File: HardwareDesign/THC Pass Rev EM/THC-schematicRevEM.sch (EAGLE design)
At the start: 55 parts, among them J1 2.1MM-PLUG-PCB-MNT, J2 DB9-MALE, J3 DB9-FEMALE, Q1 2N2222A, U1 7805T

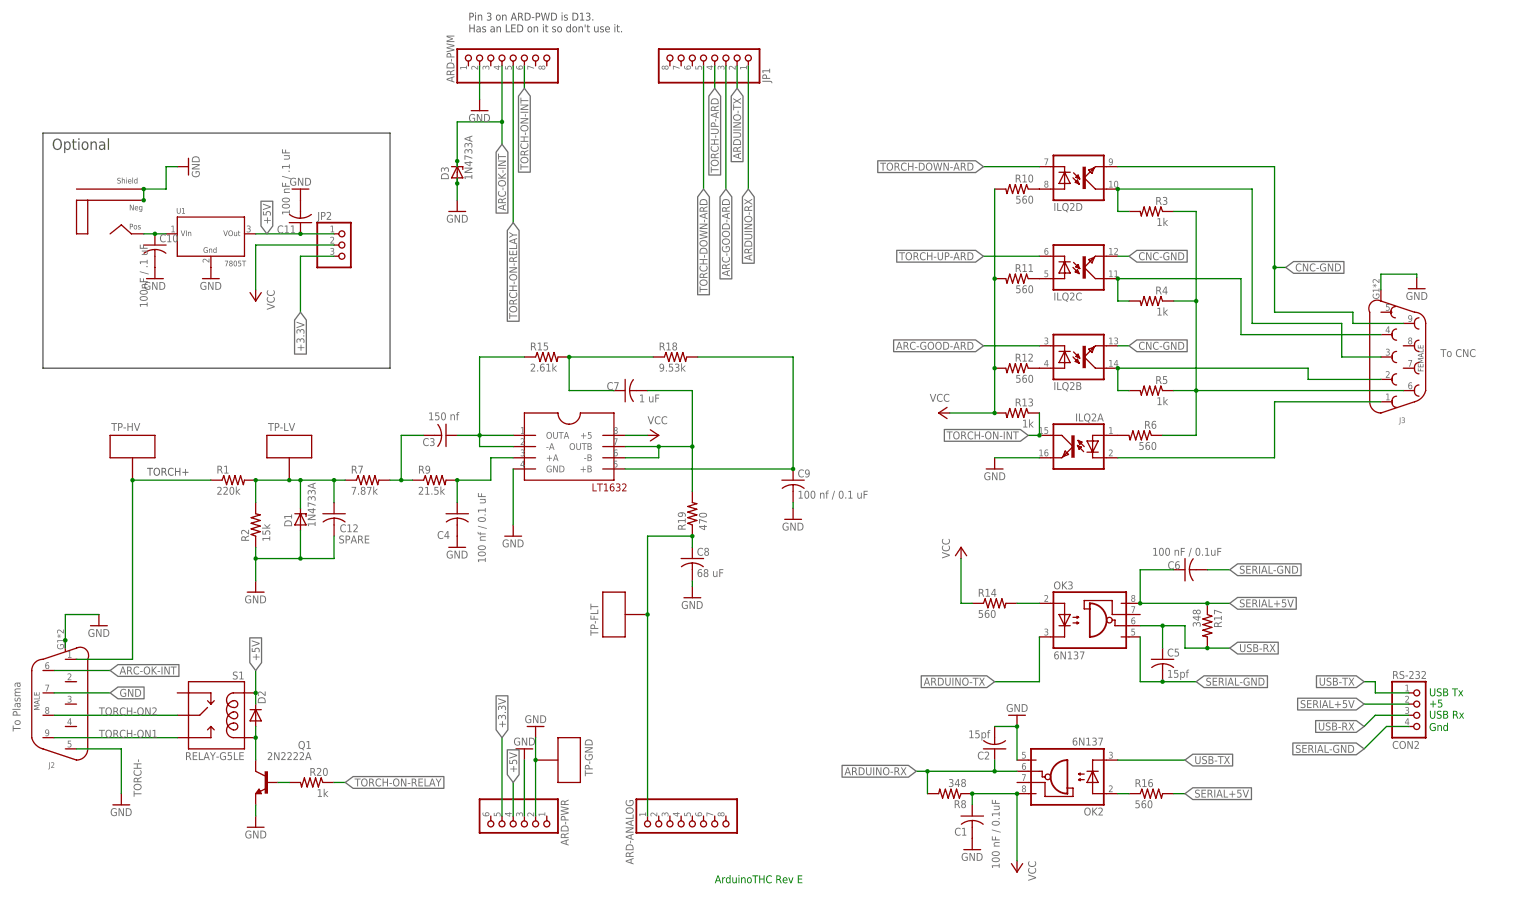
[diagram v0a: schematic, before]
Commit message: Added section to manual for programming the Arduino.  Cleaned up schematic files.
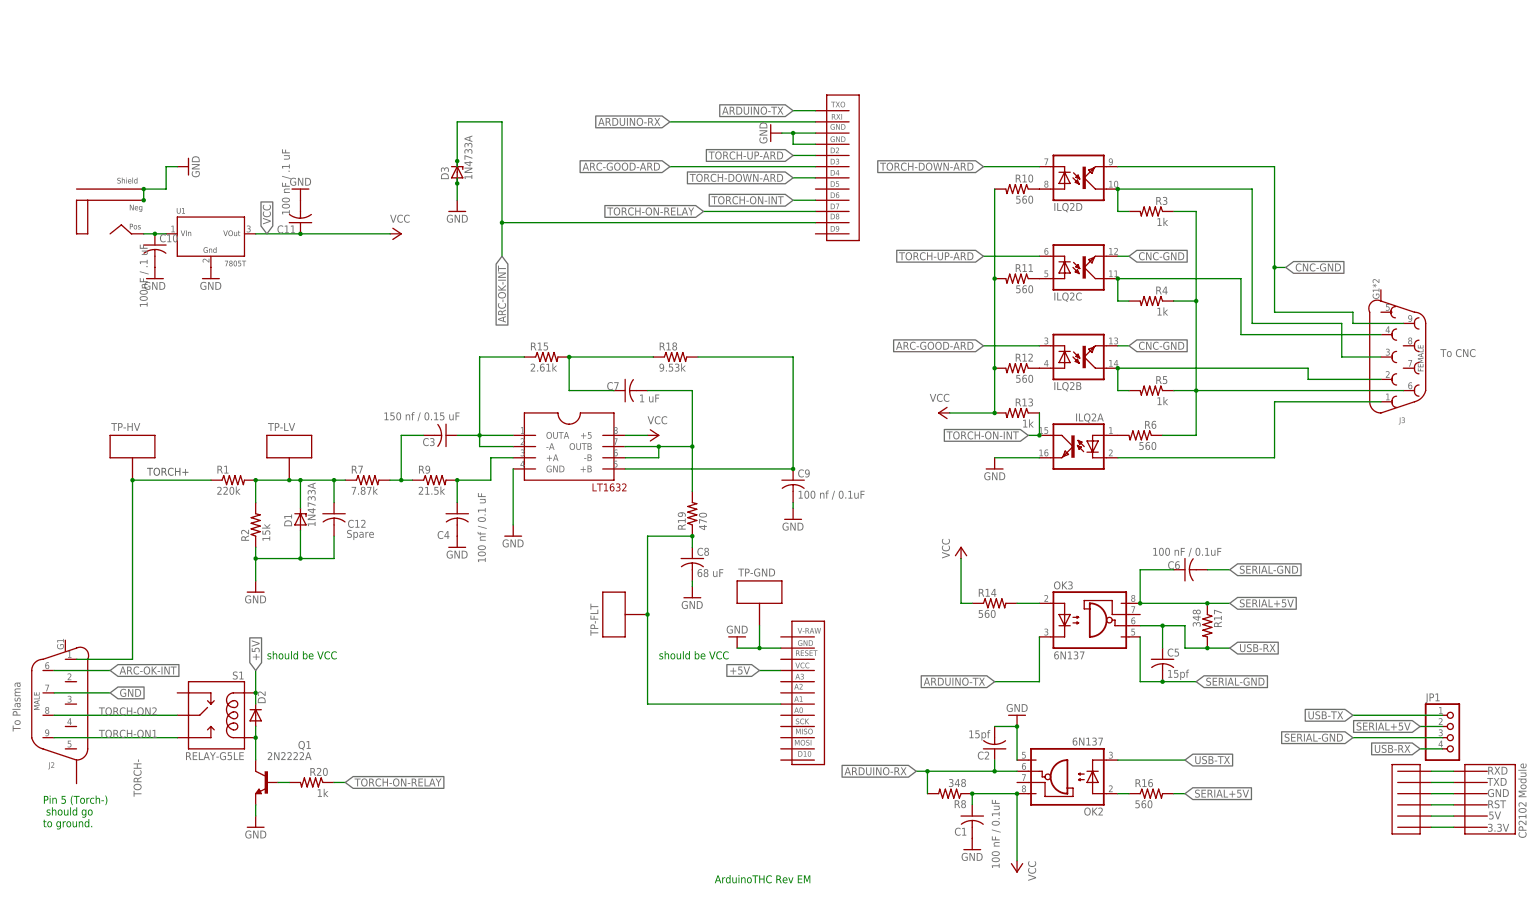
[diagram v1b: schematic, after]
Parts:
- removed ARD-ANALOG, ARD-PWM: (no value), pinhead:PINHD-1X8
- removed ARD-PWR: (no value), pinhead:PINHD-1X6
- removed JP2: (no value), pinhead:PINHD-1X3
- removed RS-232: CON2, pinhead:PINHD-1X4
- added MOD1: ARDUINO-PRO-MICRO-FOOTPRINT, ArduinoProMicro:ARDUINO-PRO-MICRO-FOOTPRINT
- added U$2: CP2102-TTL-USB, CP2102 TTL to USB:CP2102-TTL-USB
- added U$3: CP2102-PADS, CP2102 TTL to USB:CP2102-PADS
- C12: value SPARE -> Spare
- C3: value 150 nf -> 150 nf / 0.15 uF
- C9: value 100 nf / 0.1 uF -> 100 nf / 0.1uF
- JP1: device pinhead:PINHD-1X8 -> pinhead:PINHD-1X4
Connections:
- removed net +3.3V: ARD-PWR.5, JP2.3
- new net N$10: U$2.P$RST, U$3.P$RST
- new net N$11: U$2.P$TXD, U$3.P$TXD
- new net N$12: U$2.P$RXD, U$3.P$RXD
- new net N$13: U$2.P$GND, U$3.P$GND
- new net N$14: U$2.P$5V, U$3.P$5V
- new net N$6: U$2.P$3.3V, U$3.P$3.3V
- net +5V: now also MOD1G$1.VCC; no longer ARD-PWR.4, C11.1, JP2.1, U1.VOUT
- net ARC-GOOD-ARD: now also MOD1G$2.D3; no longer JP1.3
- net ARC-OK-INT: now also MOD1G$2.D8; no longer ARD-PWM.4
- net ARD-ANALOG-IN: now also MOD1G$1.A1; no longer ARD-ANALOG.1
- net ARDUINO-RX: now also MOD1G$2.RXI; no longer JP1.1
- net ARDUINO-TX: now also MOD1G$2.TX0; no longer JP1.2
- net GND: now also MOD1G$1.GND2, MOD1G$2.GND10, MOD1G$2.GND9; no longer ARD-PWM.2, ARD-PWR.2, ARD-PWR.3, J2.P$5, J2.P$SHLD, J3.P$SHLD
- net SERIAL+5V: now also JP1.2; no longer RS-232.2
- net SERIAL-GND: now also JP1.3; no longer RS-232.4
- net TORCH-DOWN-ARD: now also MOD1G$2.D4; no longer JP1.5
- net TORCH-ON-INT: now also MOD1G$2.D6; no longer ARD-PWM.6
- net TORCH-ON-RELAY: now also MOD1G$2.D7; no longer ARD-PWM.5
- net TORCH-UP-ARD: now also MOD1G$2.D2; no longer JP1.4
- net USB-RX: now also JP1.4; no longer RS-232.3
- net USB-TX: now also JP1.1; no longer RS-232.1
- net VCC: now also C11.1, U1.VOUT; no longer JP2.2
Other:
- note added: "ArduinoTHC Rev EM"
- note added: "Pin 5 (Torch-) should go to ground."
- note added: "should be VCC"
- note removed: "+5"
- note removed: "ArduinoTHC Rev E"
- note removed: "Gnd"
- note removed: "Optional"
- note removed: "Pin 3 on ARD-PWD is D13. Has an LED on it so don't use it."
- note removed: "USB Rx"
- note removed: "USB Tx"
- moved on the sheet: TP-GND
